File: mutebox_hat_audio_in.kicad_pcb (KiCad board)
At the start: 2 copper layers, 65 x 56 mm, 41 parts, among them J1 GPIO, J2 PLR237/T10BK, U1 CAT24C256, U2 74LVC157, U3 PCM1862DBT, U4 DIR9001PW, Y1 12.288 MHz

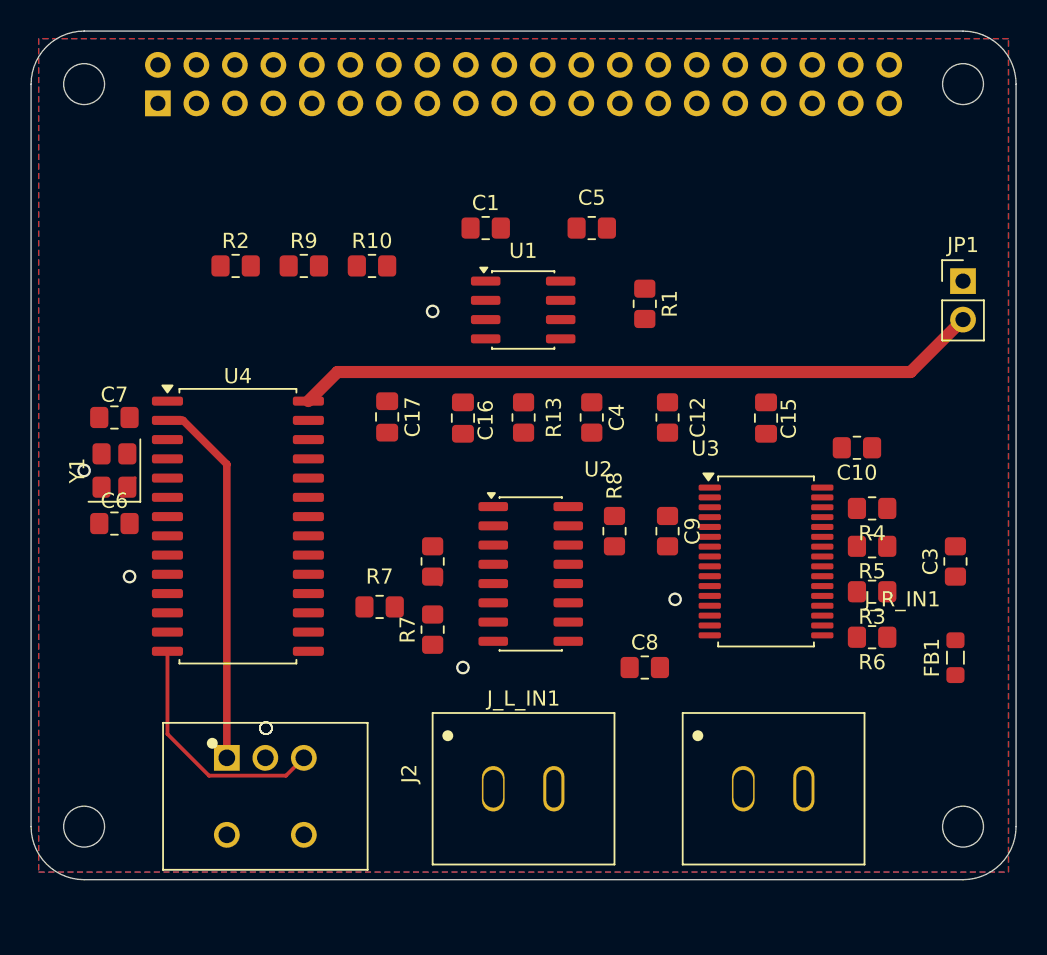
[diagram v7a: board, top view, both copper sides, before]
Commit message: Added 3v3_a traces.  rearranged some components
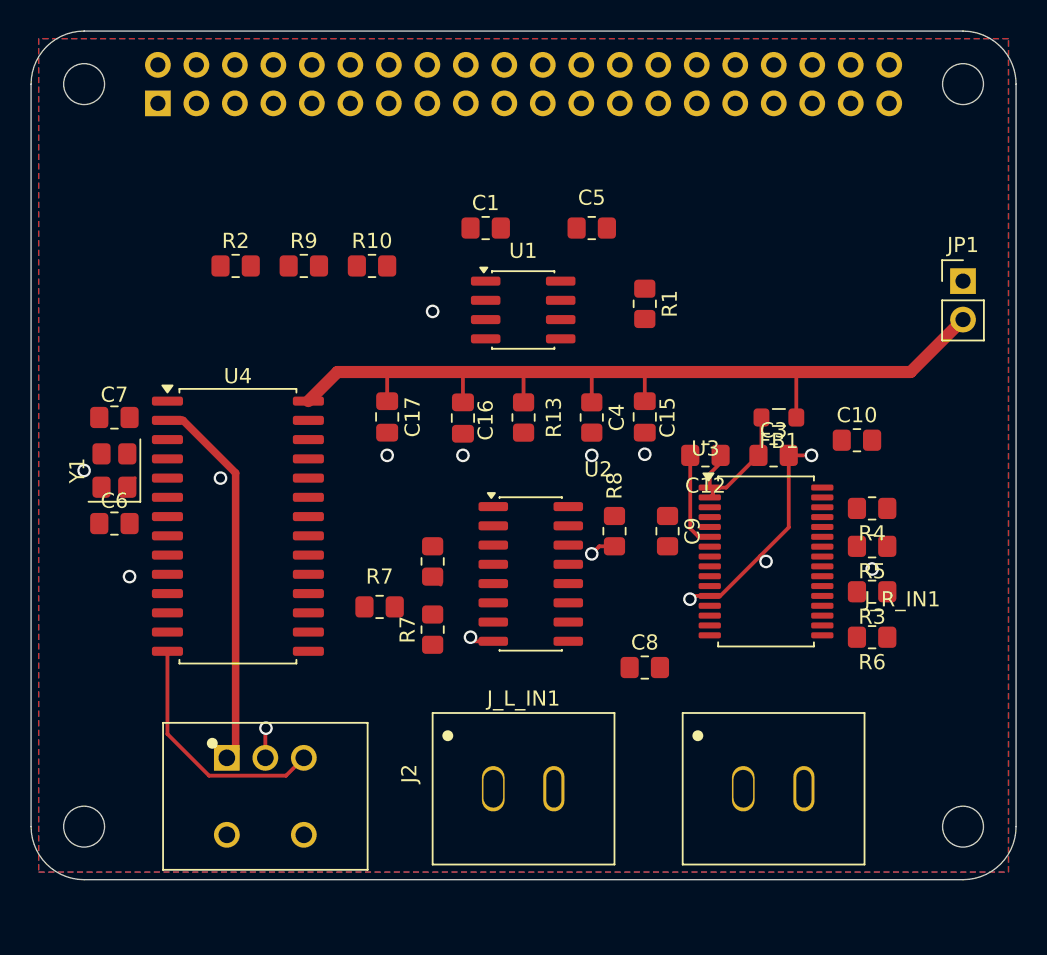
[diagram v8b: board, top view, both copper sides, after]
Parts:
- moved FB1 19.7 mm to (149.3, 69.5), turned to 180 degrees
- moved C3 13.9 mm to (149.0, 72.0), turned to 0 degrees
- moved C15 8.00 mm to (140.5, 69.5)
- moved C12 3.54 mm to (144.5, 72.0), turned to 180 degrees
- moved C10 0.50 mm to (154.5, 71.0), turned to 0 degrees
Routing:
- net GND: track 0.00 -> 20.6 mm, vias 9 -> 15
- net +3V3: track 62.3 -> 75.1 mm
- net 3V3_A: track 0.00 -> 9.42 mm
- net Net-(U3-VREF): track 0.00 -> 5.84 mm
